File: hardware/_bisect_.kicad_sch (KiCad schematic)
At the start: 29 parts

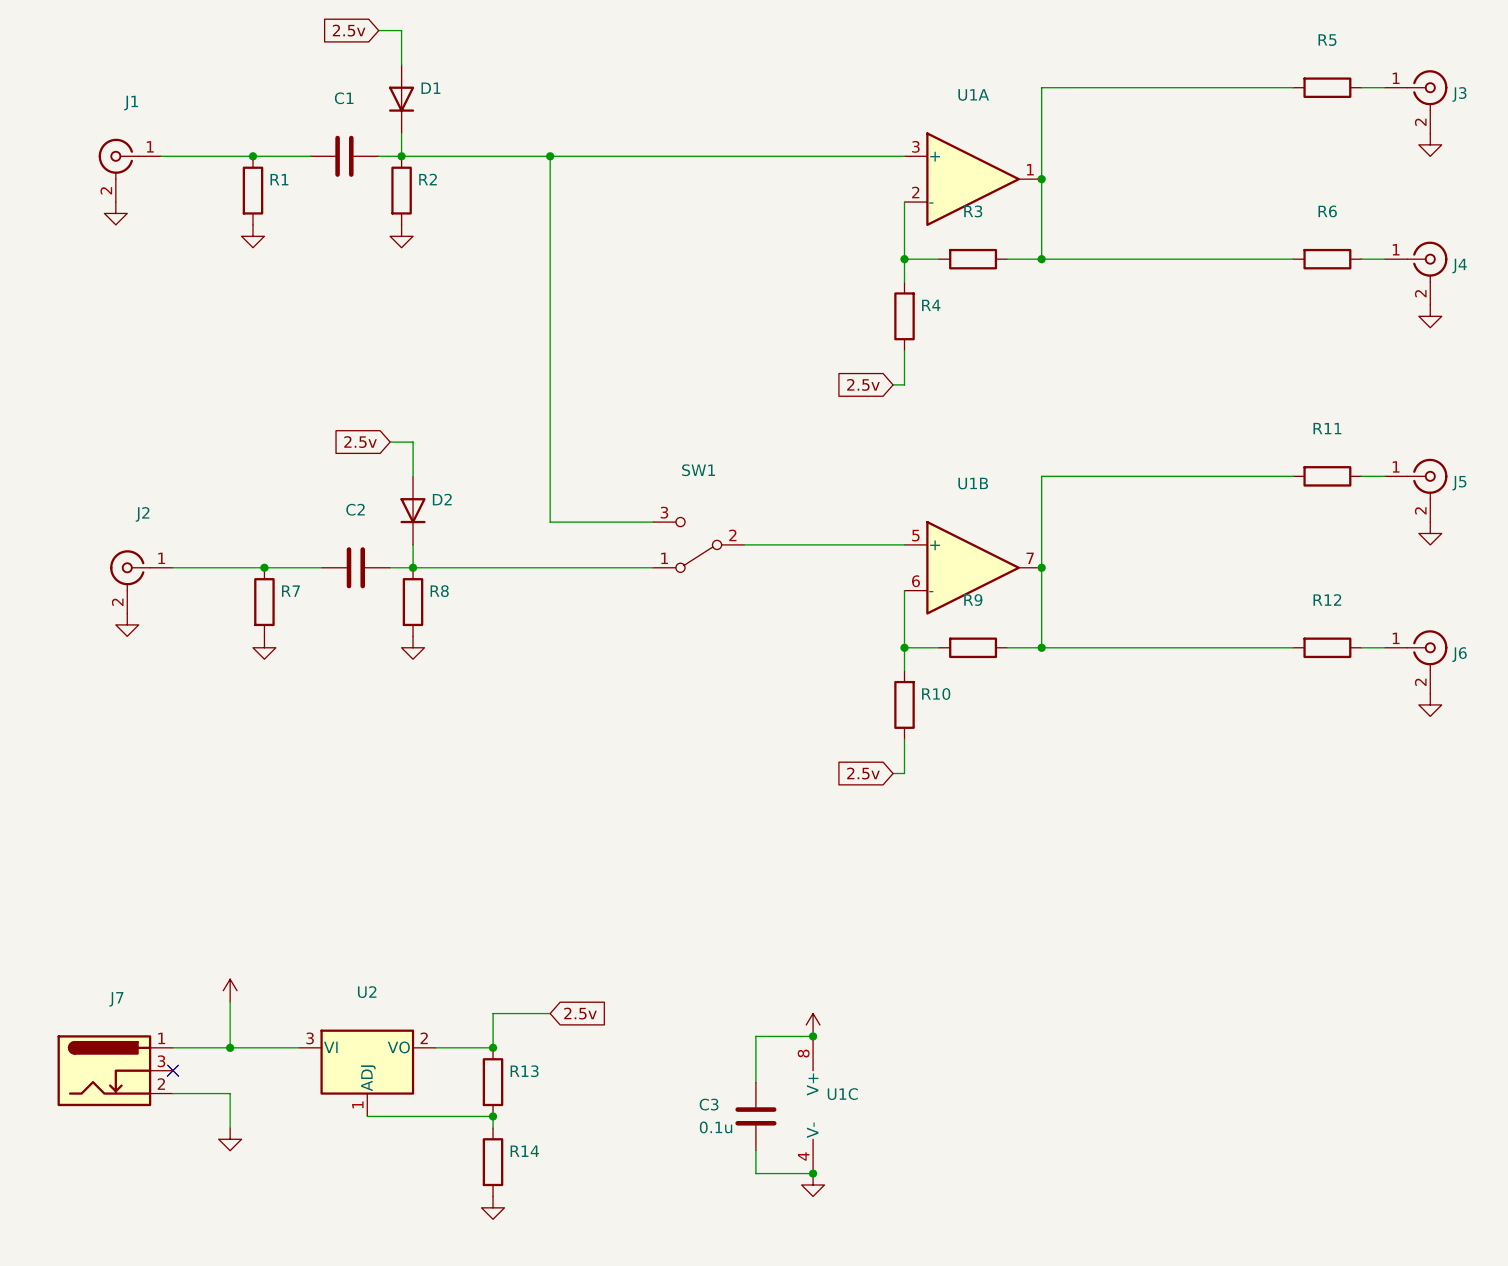
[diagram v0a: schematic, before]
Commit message: adding bom
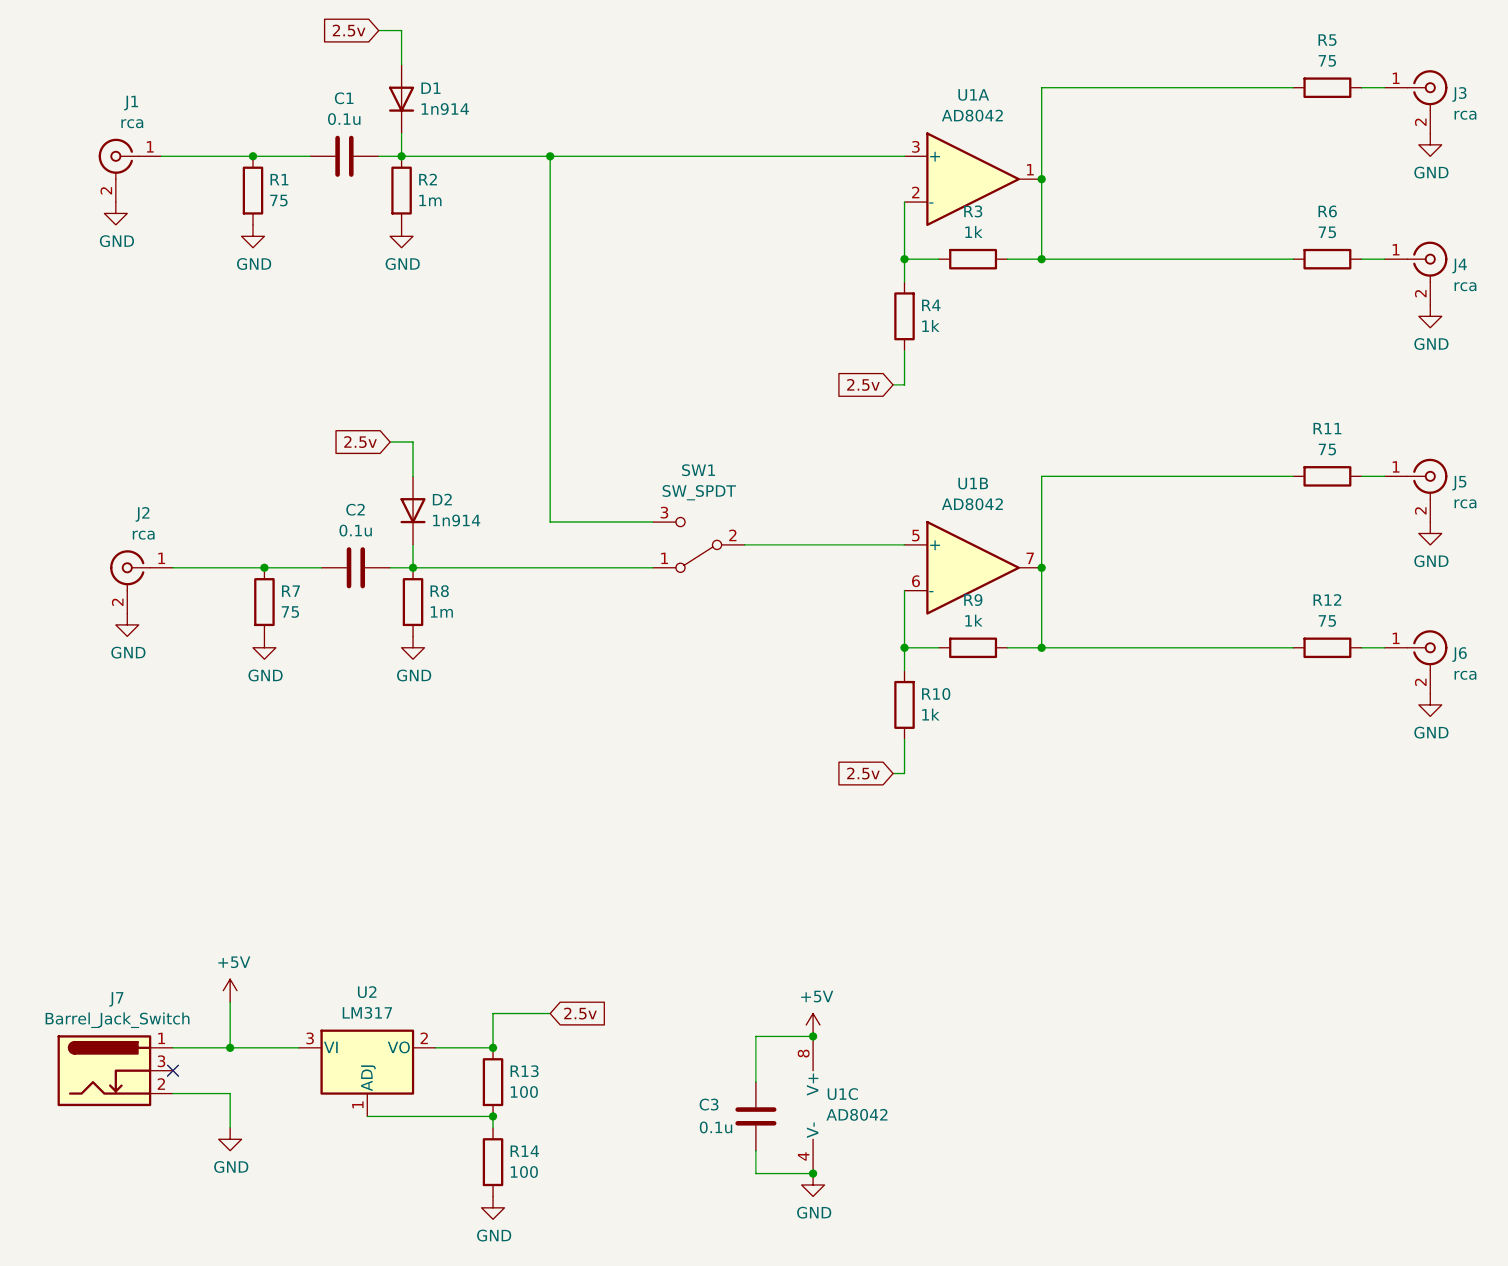
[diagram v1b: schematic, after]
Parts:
- C1, C2: value (none) -> 0.1u; footprint (none) -> Capacitor_THT:C_Disc_D4.7mm_W2.5mm_P5.00mm
- D1, D2: value (none) -> 1n914; footprint (none) -> Diode_THT:D_T-1_P5.08mm_Horizontal
- J1, J2, J3, J4, J5, J6: value (none) -> rca; footprint (none) -> lib_fp:tht_rca_vertical
- J7: value (none) -> Barrel_Jack_Switch; footprint (none) -> lib_fp:BarrelJack_Horizontal
- R1, R11, R12, R5, R6, R7: value (none) -> 75; footprint (none) -> Resistor_THT:R_Axial_DIN0207_L6.3mm_D2.5mm_P5.08mm_Vertical
- R10, R3, R4, R9: value (none) -> 1k; footprint (none) -> Resistor_THT:R_Axial_DIN0207_L6.3mm_D2.5mm_P5.08mm_Vertical
- R13, R14: value (none) -> 100; footprint (none) -> Resistor_THT:R_Axial_DIN0207_L6.3mm_D2.5mm_P5.08mm_Vertical
- R2, R8: value (none) -> 1m; footprint (none) -> Resistor_THT:R_Axial_DIN0207_L6.3mm_D2.5mm_P5.08mm_Vertical
- SW1: value (none) -> SW_SPDT; footprint (none) -> lib_fp:spdt_slide_switch_small_tayda
- U1: value (none) -> AD8042; footprint (none) -> Package_SO:SOIC-8_3.9x4.9mm_P1.27mm
- U2: value (none) -> LM317; footprint (none) -> Package_TO_SOT_THT:TO-92_HandSolder
